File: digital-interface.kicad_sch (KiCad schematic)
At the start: 23 parts, among them U32001 Si8641BD-B-IS2, U32002 R05C05TE05S

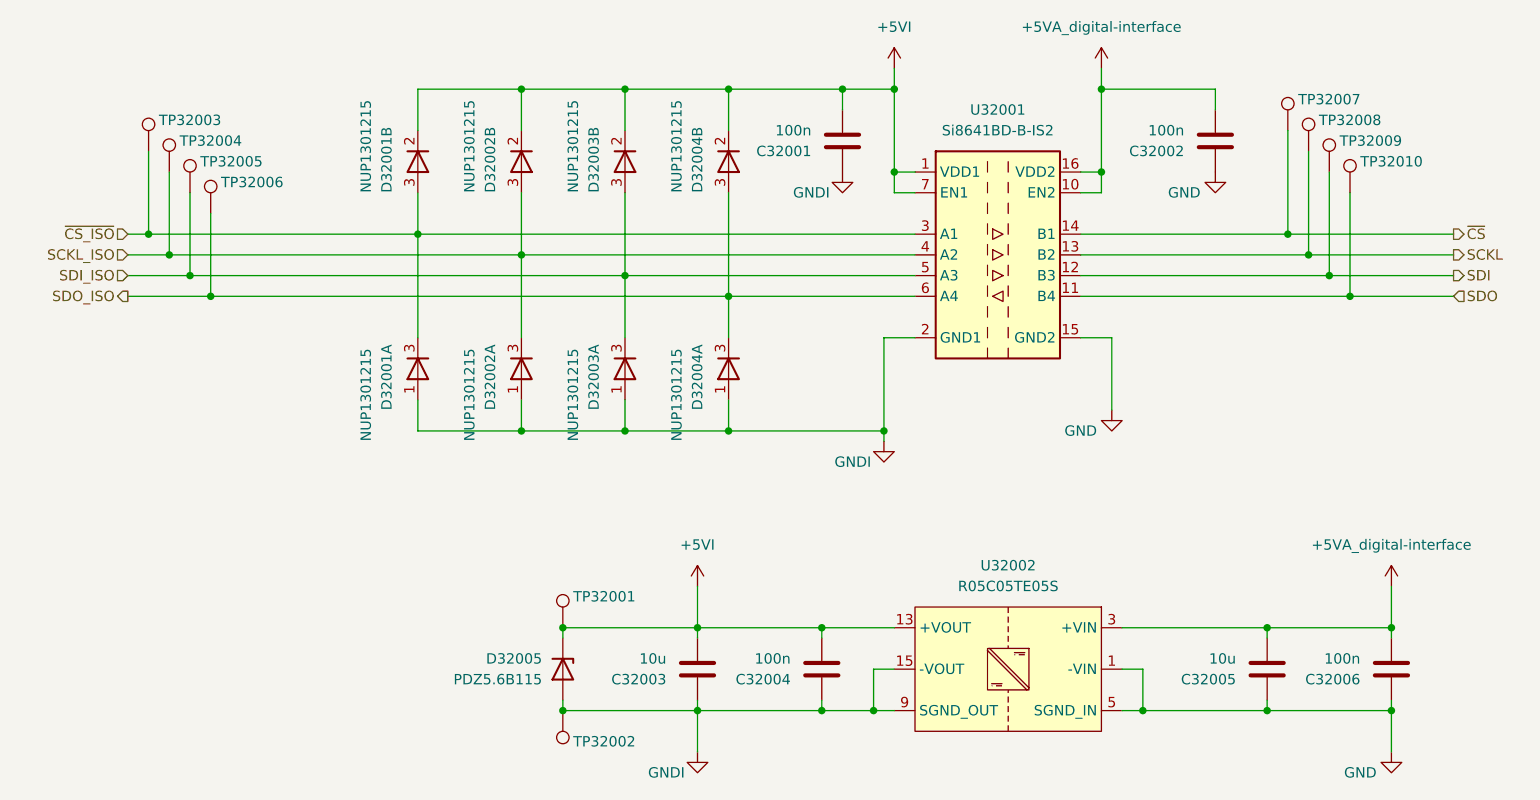
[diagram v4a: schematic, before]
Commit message: edit pss footprint library: export all footprints to library 'pss' and update footprint links
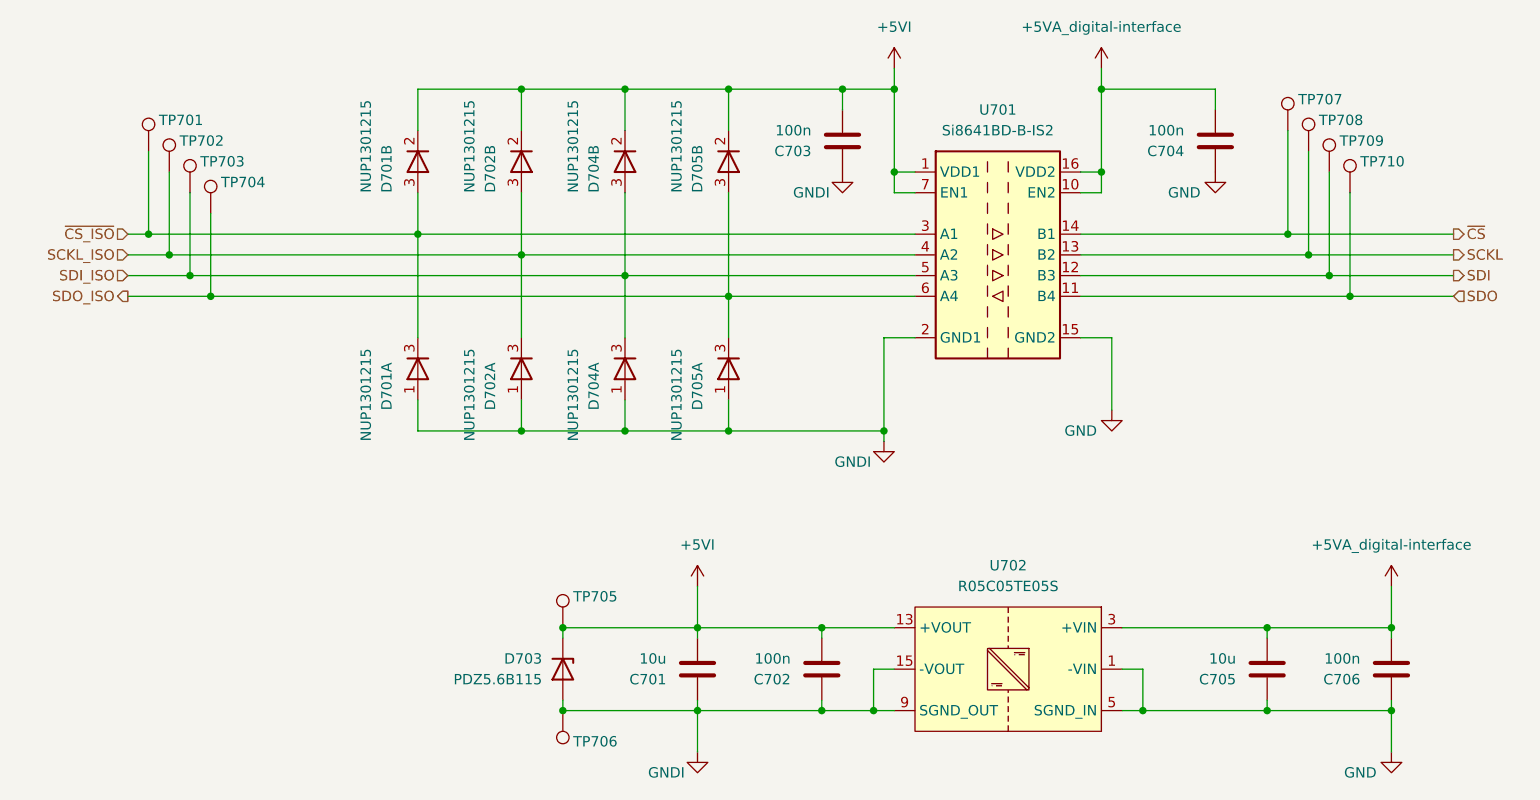
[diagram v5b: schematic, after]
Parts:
- C701: renamed from C32003; footprint Capacitor_SMD:C_1210_3225Metric_Pad1.33x2.70mm_HandSolder -> pss:C_1210_3225Metric_Pad1.33x2.70mm_HandSolder
- C702: renamed from C32004; footprint Capacitor_SMD:C_0805_2012Metric_Pad1.18x1.45mm_HandSolder -> pss:C_0805_2012Metric_Pad1.18x1.45mm_HandSolder
- C703: renamed from C32001; footprint Capacitor_SMD:C_0805_2012Metric_Pad1.18x1.45mm_HandSolder -> pss:C_0805_2012Metric_Pad1.18x1.45mm_HandSolder
- C704: renamed from C32002; footprint Capacitor_SMD:C_0805_2012Metric_Pad1.18x1.45mm_HandSolder -> pss:C_0805_2012Metric_Pad1.18x1.45mm_HandSolder
- C705: renamed from C32005; footprint Capacitor_SMD:C_1210_3225Metric_Pad1.33x2.70mm_HandSolder -> pss:C_1210_3225Metric_Pad1.33x2.70mm_HandSolder
- C706: renamed from C32006; footprint Capacitor_SMD:C_0805_2012Metric_Pad1.18x1.45mm_HandSolder -> pss:C_0805_2012Metric_Pad1.18x1.45mm_HandSolder
- D701: renamed from D32001; footprint Package_TO_SOT_SMD:SOT-23_Handsoldering -> pss:SOT-23_Handsoldering
- D702: renamed from D32002; footprint Package_TO_SOT_SMD:SOT-23_Handsoldering -> pss:SOT-23_Handsoldering
- D703: renamed from D32005; footprint Diode_SMD:D_SOD-323_HandSoldering -> pss:D_SOD-323_HandSoldering
- D704: renamed from D32003; footprint Package_TO_SOT_SMD:SOT-23_Handsoldering -> pss:SOT-23_Handsoldering
- D705: renamed from D32004; footprint Package_TO_SOT_SMD:SOT-23_Handsoldering -> pss:SOT-23_Handsoldering
- U701: renamed from U32001; footprint Package_SO:SOIC-16W_7.5x10.3mm_P1.27mm -> pss:SOIC-16W_7.5x10.3mm_P1.27mm
- U702: renamed from U32002; footprint Package_SO:SOIC-16W_7.5x10.3mm_P1.27mm -> pss:SOIC-16W_7.5x10.3mm_P1.27mm
- renumbered TP32003 to TP701, TP32004 to TP702, TP32005 to TP703, TP32006 to TP704, TP32001 to TP705, TP32002 to TP706, TP32007 to TP707, TP32008 to TP708, TP32009 to TP709, TP32010 to TP710
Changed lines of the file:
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@@
 		(on_board yes)
 		(dnp no)
-		(property "Reference" "C32006"
+		(property "Reference" "C706"
 			(at 191.77 123.1901 0)
 			(effects
@@
 			)
 		)
-		(property "Footprint" "Capacitor_SMD:C_0805_2012Metric_Pad1.18x1.45mm_HandSolder"
+		(property "Footprint" "pss:C_0805_2012Metric_Pad1.18x1.45mm_HandSolder"
 			(at 194.6148 118.11 0)
 			(effects
@@
 		(on_board yes)
 		(dnp no)
-		(property "Reference" "TP32005"
+		(property "Reference" "TP703"
 			(at 49.53 59.69 0)
 			(effects
@@
 		(on_board yes)
 		(dnp no)
-		(property "Reference" "D32004"
+		(property "Reference" "D705"
 			(at 110.49 90.17 0)
 			(effects
@@
 			)
 		)
-		(property "Footprint" "Package_TO_SOT_SMD:SOT-23_Handsoldering"
+		(property "Footprint" "pss:SOT-23_Handsoldering"
 			(at 116.84 87.63 0)
 			(effects
@@
 		(on_board yes)
 		(dnp no)
-		(property "Reference" "TP32008"
+		(property "Reference" "TP708"
 			(at 186.69 54.61 0)
 			(effects
@@
 		(on_board yes)
 		(dnp no)
-		(property "Reference" "#PWR032004"
+		(property "Reference" "#PWR0704"
 			(at 133.35 100.33 0)
 			(effects
@@
 		(on_board yes)
 		(dnp no)
-		(property "Reference" "C32002"
+		(property "Reference" "C704"
 			(at 170.18 58.4201 0)
 			(effects
@@
 			)
 		)
-		(property "Footprint" "Capacitor_SMD:C_0805_2012Metric_Pad1.18x1.45mm_HandSolder"
+		(property "Footprint" "pss:C_0805_2012Metric_Pad1.18x1.45mm_HandSolder"
 			(at 173.0248 53.34 0)
 			(effects
@@
 		(dnp no)
 		(fields_autoplaced yes)
-		(property "Reference" "#PWR032007"
+		(property "Reference" "#PWR0709"
 			(at 195.58 115.57 0)
 			(effects
@@
 		(on_board yes)
 		(dnp no)
-		(property "Reference" "TP32003"
+		(property "Reference" "TP701"
 			(at 44.45 54.61 0)
 			(effects
@@
 		(dnp no)
 		(fields_autoplaced yes)
-		(property "Reference" "#PWR032001"
+		(property "Reference" "#PWR0706"
 			(at 160.02 52.07 0)
 			(effects
@@
 		(on_board yes)
 		(dnp no)
-		(property "Reference" "D32001"
+		(property "Reference" "D701"
 			(at 72.39 63.5 0)
 			(effects
@@
 			)
 		)
-		(property "Footprint" "Package_TO_SOT_SMD:SOT-23_Handsoldering"
+		(property "Footprint" "pss:SOT-23_Handsoldering"
 			(at 73.66 57.15 0)
 			(effects
@@
 		(on_board yes)
 		(dnp no)
-		(property "Reference" "D32002"
+		(property "Reference" "D702"
 			(at 85.09 63.5 0)
 			(effects
@@
 			)
 		)
-		(property "Footprint" "Package_TO_SOT_SMD:SOT-23_Handsoldering"
+		(property "Footprint" "pss:SOT-23_Handsoldering"
 			(at 86.36 57.15 0)
 			(effects
@@
 		(on_board yes)
 		(dnp no)
-		(property "Reference" "C32005"
+		(property "Reference" "C705"
 			(at 176.53 123.1901 0)
 			(effects
@@
 			)
 		)
-		(property "Footprint" "Capacitor_SMD:C_1210_3225Metric_Pad1.33x2.70mm_HandSolder"
+		(property "Footprint" "pss:C_1210_3225Metric_Pad1.33x2.70mm_HandSolder"
 			(at 179.3748 118.11 0)
 			(effects
@@
 		(on_board yes)
 		(dnp no)
-		(property "Reference" "D32004"
+		(property "Reference" "D705"
 			(at 110.49 63.5 0)
 			(effects
@@
 			)
 		)
-		(property "Footprint" "Package_TO_SOT_SMD:SOT-23_Handsoldering"
+		(property "Footprint" "pss:SOT-23_Handsoldering"
 			(at 111.76 57.15 0)
 			(effects
@@
 		(on_board yes)
 		(dnp no)
-		(property "Reference" "#PWR032008"
+		(property "Reference" "#PWR0710"
 			(at 195.58 138.43 0)
 			(effects
@@
 		(on_board yes)
 		(dnp no)
-		(property "Reference" "TP32010"
+		(property "Reference" "TP710"
 			(at 191.77 59.69 0)
 			(effects
@@
 		(on_board yes)
 		(dnp no)
-		(property "Reference" "D32005"
+		(property "Reference" "D703"
 			(at 91.44 120.6499 90)
 			(effects
@@
 			)
 		)
-		(property "Footprint" "Diode_SMD:D_SOD-323_HandSoldering"
+		(property "Footprint" "pss:D_SOD-323_HandSoldering"
 			(at 93.98 121.92 0)
 			(effects
@@
 		(dnp no)
 		(fields_autoplaced yes)
-		(property "Reference" "#PWR032010"
+		(property "Reference" "#PWR0701"
 			(at 110.49 115.57 0)
 			(effects
@@
 		(dnp no)
 		(fields_autoplaced yes)
-		(property "Reference" "#PWR032005"
+		(property "Reference" "#PWR0705"
 			(at 134.62 52.07 0)
 			(effects
@@
 		(on_board yes)
 		(dnp no)
-		(property "Reference" "#PWR032009"
+		(property "Reference" "#PWR0702"
 			(at 110.49 138.43 0)
 			(effects
@@
 		(on_board yes)
 		(dnp no)
-		(property "Reference" "TP32006"
+		(property "Reference" "TP704"
 			(at 52.07 62.23 0)
 			(effects
@@
 		(on_board yes)
 		(dnp no)
-		(property "Reference" "C32003"
+		(property "Reference" "C701"
 			(at 106.68 123.1901 0)
 			(effects
@@
 			)
 		)
-		(property "Footprint" "Capacitor_SMD:C_1210_3225Metric_Pad1.33x2.70mm_HandSolder"
+		(property "Footprint" "pss:C_1210_3225Metric_Pad1.33x2.70mm_HandSolder"
 			(at 109.5248 118.11 0)
 			(effects
@@
 		(on_board yes)
 		(dnp no)
-		(property "Reference" "TP32009"
+		(property "Reference" "TP709"
 			(at 189.23 57.15 0)
 			(effects
@@
 		(on_board yes)
 		(dnp no)
-		(property "Reference" "D32002"
+		(property "Reference" "D702"
 			(at 85.09 90.17 0)
 			(effects
@@
 			)
 		)
-		(property "Footprint" "Package_TO_SOT_SMD:SOT-23_Handsoldering"
+		(property "Footprint" "pss:SOT-23_Handsoldering"
 			(at 91.44 87.63 0)
 			(effects
@@
 		(on_board yes)
 		(dnp no)
-		(property "Reference" "U32002"
+		(property "Reference" "U702"
 			(at 148.59 109.22 0)
 			(effects
@@
 			)
 		)
-		(property "Footprint" "Package_SO:SOIC-16W_7.5x10.3mm_P1.27mm"
+		(property "Footprint" "pss:SOIC-16W_7.5x10.3mm_P1.27mm"
 			(at 148.59 121.92 0)
 			(effects
@@
 		(on_board yes)
 		(dnp no)
-		(property "Reference" "D32003"
+		(property "Reference" "D704"
 			(at 97.79 90.17 0)
 			(effects
@@
 			)
 		)
-		(property "Footprint" "Package_TO_SOT_SMD:SOT-23_Handsoldering"
+		(property "Footprint" "pss:SOT-23_Handsoldering"
 			(at 104.14 87.63 0)
 			(effects
@@
 		(on_board yes)
 		(dnp no)
-		(property "Reference" "TP32001"
+		(property "Reference" "TP705"
 			(at 95.25 113.03 0)
 			(effects
@@
 		(on_board yes)
 		(dnp no)
-		(property "Reference" "#PWR032003"
+		(property "Reference" "#PWR0707"
 			(at 161.29 96.52 0)
 			(effects
@@
 		(on_board yes)
 		(dnp no)
-		(property "Reference" "#PWR032002"
+		(property "Reference" "#PWR0708"
 			(at 173.99 67.31 0)
 			(effects
@@
 		(on_board yes)
 		(dnp no)
-		(property "Reference" "TP32004"
+		(property "Reference" "TP702"
 			(at 46.99 57.15 0)
 			(effects
@@
 		(on_board yes)
 		(dnp no)
-		(property "Reference" "C32004"
+		(property "Reference" "C702"
 			(at 121.92 123.1901 0)
 			(effects
@@
 			)
 		)
-		(property "Footprint" "Capacitor_SMD:C_0805_2012Metric_Pad1.18x1.45mm_HandSolder"
+		(property "Footprint" "pss:C_0805_2012Metric_Pad1.18x1.45mm_HandSolder"
 			(at 124.7648 118.11 0)
 			(effects
@@
 		(on_board yes)
 		(dnp no)
-		(property "Reference" "TP32007"
+		(property "Reference" "TP707"
 			(at 184.15 52.07 0)
 			(effects
@@
 		(on_board yes)
 		(dnp no)
-		(property "Reference" "TP32002"
+		(property "Reference" "TP706"
 			(at 95.25 130.81 0)
 			(effects
@@
 		(on_board yes)
 		(dnp no)
-		(property "Reference" "#PWR032006"
+		(property "Reference" "#PWR0703"
 			(at 128.27 67.31 0)
 			(effects
@@
 		(on_board yes)
 		(dnp no)
-		(property "Reference" "D32001"
+		(property "Reference" "D701"
 			(at 72.39 90.17 0)
 			(effects
@@
 			)
 		)
-		(property "Footprint" "Package_TO_SOT_SMD:SOT-23_Handsoldering"
+		(property "Footprint" "pss:SOT-23_Handsoldering"
 			(at 78.74 87.63 0)
 			(effects
@@
 		(on_board yes)
 		(dnp no)
-		(property "Reference" "D32003"
+		(property "Reference" "D704"
 			(at 97.79 63.5 0)
 			(effects
@@
 			)
 		)
-		(property "Footprint" "Package_TO_SOT_SMD:SOT-23_Handsoldering"
+		(property "Footprint" "pss:SOT-23_Handsoldering"
 			(at 99.06 57.15 0)
 			(effects
@@
 		(dnp no)
 		(fields_autoplaced yes)
-		(property "Reference" "U32001"
+		(property "Reference" "U701"
 			(at 147.32 53.34 0)
 			(effects
@@
 			)
 		)
-		(property "Footprint" "Package_SO:SOIC-16W_7.5x10.3mm_P1.27mm"
+		(property "Footprint" "pss:SOIC-16W_7.5x10.3mm_P1.27mm"
 			(at 147.32 85.09 0)
 			(effects
@@
 		(on_board yes)
 		(dnp no)
-		(property "Reference" "C32001"
+		(property "Reference" "C703"
 			(at 124.46 58.4201 0)
 			(effects
@@
 			)
 		)
-		(property "Footprint" "Capacitor_SMD:C_0805_2012Metric_Pad1.18x1.45mm_HandSolder"
+		(property "Footprint" "pss:C_0805_2012Metric_Pad1.18x1.45mm_HandSolder"
 			(at 127.3048 53.34 0)
 			(effects
